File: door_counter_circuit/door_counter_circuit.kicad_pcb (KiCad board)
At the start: 4 copper layers, 99.1 x 99.1 mm, 36 parts, among them J1 Conn_01x20_Male, J2 Conn_01x20_Male, J3 Prototype_Space, Q1 BC807, SW1 SW_Push, SW2 RotaryEncoder_Switch, SW3 SW_Push, U1 Pico, U2 TSDP341xx, U3 TSDP341xx, U4 OLED_display_module, U5 DS1302+, Y1 32.768kHz

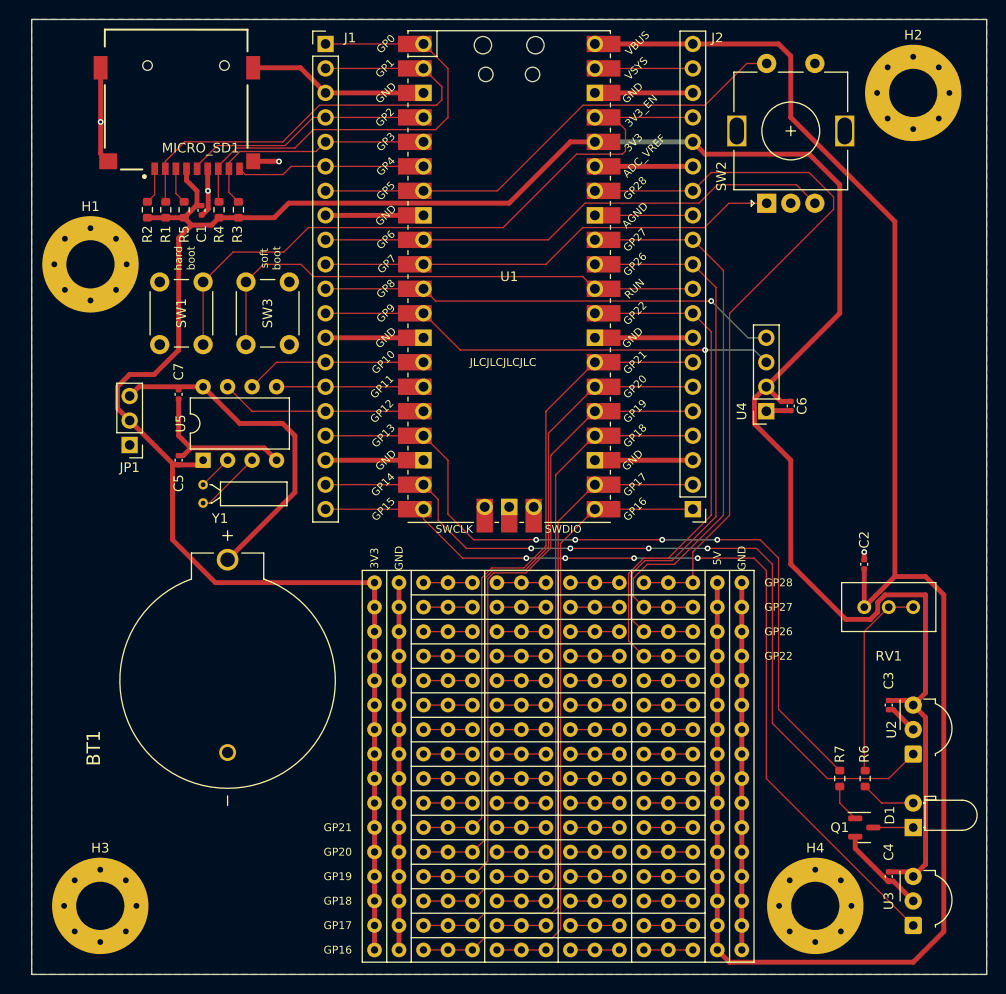
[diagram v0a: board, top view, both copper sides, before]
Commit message: include a configurable transistor footprint
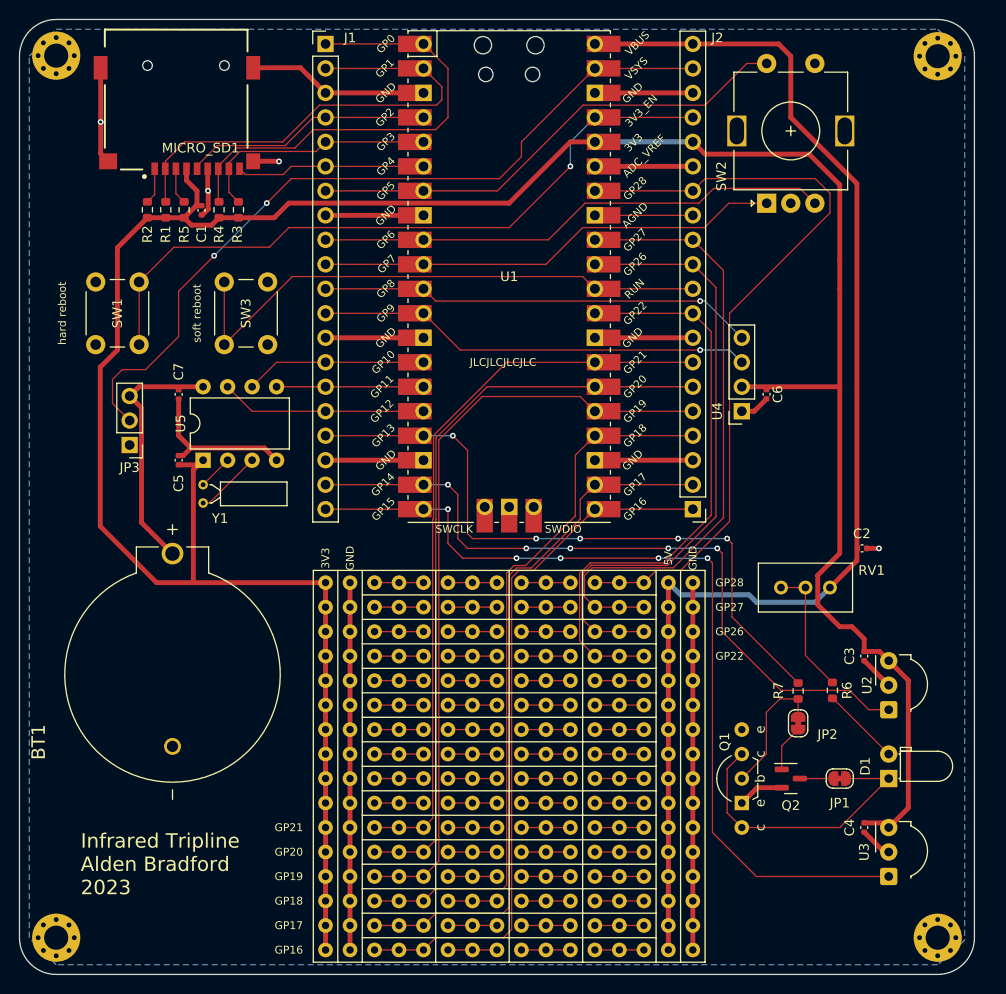
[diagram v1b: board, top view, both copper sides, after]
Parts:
- added JP1: SolderJumper_2_Bridged, Jumper:SolderJumper-2_P1.3mm_Bridged_RoundedPad1.0x1.5mm, F.Cu at (157.5, 129.5)
- added JP2: SolderJumper_2_Bridged, Jumper:SolderJumper-2_P1.3mm_Bridged_RoundedPad1.0x1.5mm, F.Cu at (153.2, 123.8)
- added Q1: ConfigurableNPN, Library:TO-92-configurable, F.Cu at (147.3, 132.1)
- H1, H2, H3, H4: footprint MountingHole:MountingHole_5mm_Pad_Via -> MountingHole:MountingHole_2.5mm_Pad_Via
- moved H1 21.9 mm to (76.2, 54.6)
- moved H4 13.1 mm to (167.6, 146.1)
- moved R7 10.1 mm to (153.2, 120.5)
- moved R6 9.76 mm to (156.7, 120.4)
- moved Q2 9.16 mm to (152.4, 129.5)
- moved SW1 6.64 mm to (84.8, 78.0)
- moved BT1 5.75 mm to (88.3, 116.2)
- moved D1 5.68 mm to (162.6, 129.5)
- moved U3 5.68 mm to (162.6, 139.7)
- moved C3 5.68 mm to (160.0, 116.8)
- moved C4 5.68 mm to (160.0, 134.6)
- moved H3 5.64 mm to (76.2, 146.1)
- moved U2 5.25 mm to (162.6, 122.4)
- moved J3 5.08 mm to (104.1, 147.3)
- moved H2 4.58 mm to (167.6, 54.6)
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- renumbered JP1 to JP3, Q1 to Q2
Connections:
- J2 pad 19: Net-(J2-Pad19) -> VSYS
- JP3 pad 2: +3V3 -> VSYS
- Q2 pad 1: Net-(Q1-Pad1) -> Net-(Q2-Pad1)
- Q2 pad 3: Net-(D1-Pad1) -> Net-(Q2-Pad3)
- R7 pad 2: Net-(Q1-Pad1) -> Net-(R7-Pad2)
- U1 pad 39: Net-(J2-Pad19) -> VSYS
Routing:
- net VSYS: track 0.00 -> 82.2 mm, vias 0 -> 2
- net +5V: track 192.0 -> 136.3 mm
- net Net-(D1-Pad1): track 4.14 -> 30.7 mm
- net Net-(R7-Pad2): track 0.00 -> 13.7 mm
- net IR_CONTROL: track 80.2 -> 69.2 mm, vias 4 -> 5
- net Net-(J2-Pad19): track 10.2 -> 0.00 mm
- net IR_DETECT_1: track 85.6 -> 75.5 mm, vias 4 -> 5
- net Net-(BT1-Pad+): track 35.4 -> 26.2 mm
- net C4: track 70.7 -> 79.9 mm
- net Net-(RV1-Pad2): track 20.6 -> 13.5 mm
- net C5: track 70.7 -> 77.4 mm
- net C6: track 70.7 -> 76.2 mm
- net M15: track 60.6 -> 66.0 mm
- net +3V3: track 290.1 -> 284.9 mm
- net M14: track 60.2 -> 65.3 mm
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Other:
- outline, holes or cut-outs redrawn
- board text added: "Infrared Tripline Alden Bradford 2023"
- board text added: "hard reboot"
- board text added: "soft reboot"
- board text removed: "hard boot"
- board text removed: "soft boot"

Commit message: manufacturing outputs
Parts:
- added FID1: Fiducial, Fiducial:Fiducial_1mm_Mask2mm, F.Cu at (162.6, 54.4)
- added FID2: Fiducial, Fiducial:Fiducial_1mm_Mask2mm, F.Cu at (76.7, 59.4)
- added FID3: Fiducial, Fiducial:Fiducial_1mm_Mask2mm, F.Cu at (76.2, 141.2)
- added FID4: Fiducial, Fiducial:Fiducial_1mm_Mask2mm, F.Cu at (162.6, 145.8)
- added TP1: TestPoint, TestPoint:TestPoint_Pad_4.0x4.0mm, F.Cu at (167.1, 63.5)
- added TP2: TestPoint, TestPoint:TestPoint_Pad_4.0x4.0mm, F.Cu at (89.6, 144.8)
- added TP3: TestPoint, TestPoint:TestPoint_Pad_4.0x4.0mm, F.Cu at (157.2, 145.8)
- Q1: renamed from Q2; value BC807 -> MMS9013-H-TP
- R7: renamed from R6; footprint Resistor_SMD:R_0603_1608Metric -> Resistor_SMD:R_0805_2012Metric
- moved J2 5.08 mm to (137.2, 101.6)
- moved U2 5.08 mm to (142.2, 91.4)
- moved C3 4.85 mm to (145.0, 89.7)
- moved U1 2.54 mm to (120.7, 77.5)
- renumbered C7 to C2, C6 to C3, C5 to C4, C2 to C5, C3 to C6, C4 to C7, JP3 to JP1, JP1 to JP3, Q1 to Q2, R2 to R1, R1 to R2, R5 to R3, R3 to R5, R7 to R6, SW2 to SW1, SW1 to SW2, U4 to U2, U5 to U3, U2 to U4, U3 to U5
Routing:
- net GND: track 206.3 -> 217.6 mm
- net C4: track 79.9 -> 70.1 mm
- net C5: track 77.4 -> 69.4 mm
- net C6: track 76.2 -> 68.6 mm
- net M15: track 66.0 -> 59.0 mm
- net M14: track 65.3 -> 59.0 mm
- net M13: track 62.4 -> 56.4 mm
- net +3V3: track 284.9 -> 290.0 mm
- net Net-(J2-Pad10): track 58.6 -> 53.5 mm
- net OLED_SCL: track 45.3 -> 40.2 mm
- net OLED_SDA: track 45.3 -> 40.2 mm
- net VSYS: track 82.2 -> 77.3 mm
- net IR_CONTROL: track 69.2 -> 64.4 mm, vias 5 -> 1
- net C2: track 73.3 -> 68.8 mm
- net C1: track 73.3 -> 68.8 mm
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
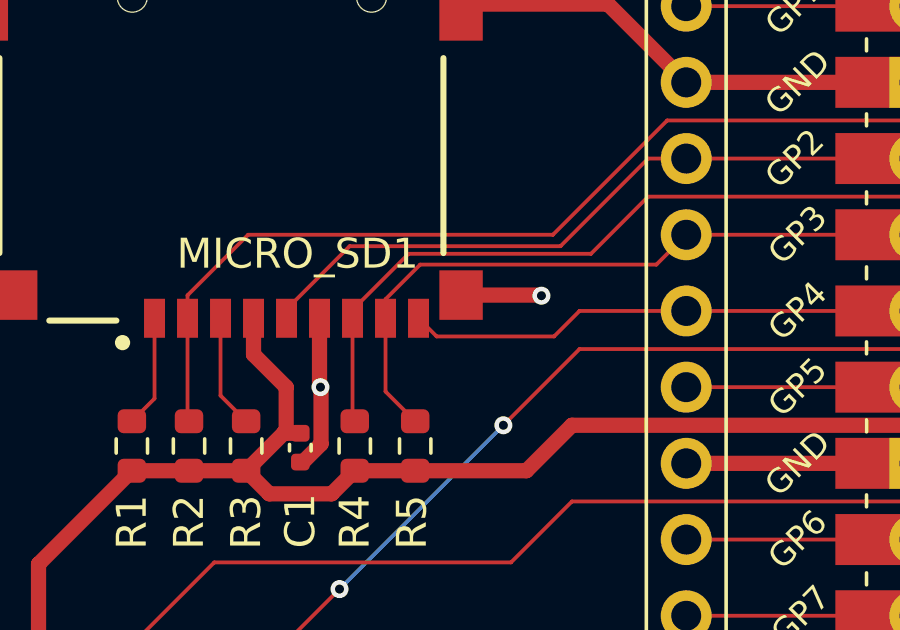
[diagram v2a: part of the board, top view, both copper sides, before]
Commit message: fix to SD circuit
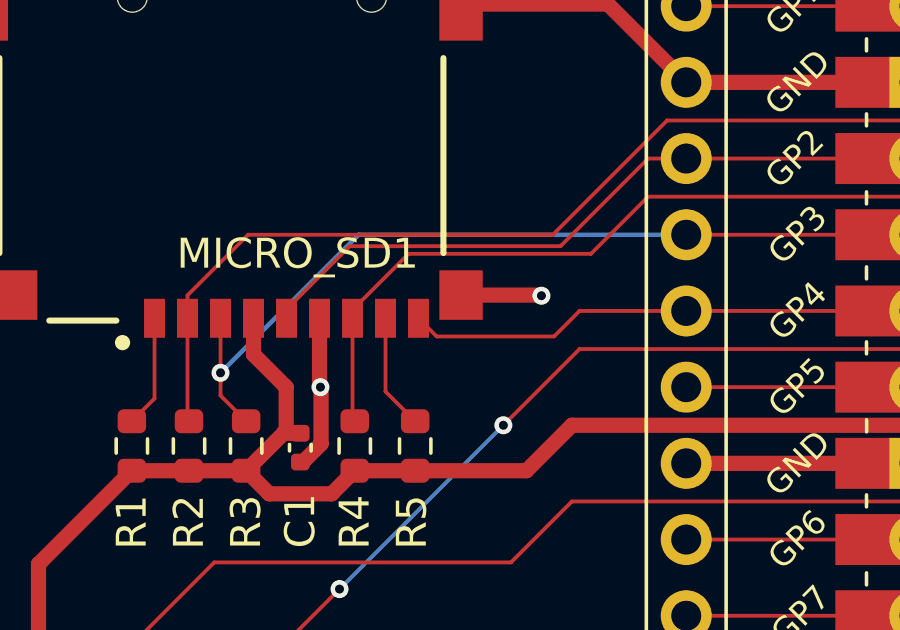
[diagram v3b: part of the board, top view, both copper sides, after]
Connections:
- MICRO_SD1 pad 3: Net-(MICRO_SD1-Pad3) -> SD_MOSI
- MICRO_SD1 pad 8: SD_MOSI -> Net-(MICRO_SD1-Pad8)
- R3 pad 2: Net-(MICRO_SD1-Pad3) -> SD_MOSI
- R5 pad 2: SD_MOSI -> Net-(MICRO_SD1-Pad8)
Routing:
- net SD_MOSI: track 23.0 -> 28.8 mm, vias 0 -> 1
- net Net-(MICRO_SD1-Pad8): track 0.00 -> 3.84 mm
- net Net-(MICRO_SD1-Pad3): track 3.79 -> 0.00 mm
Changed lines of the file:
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@@
   (net 34 "SD_CS")
   (net 35 "Net-(MICRO_SD1-Pad1)")
-  (net 36 "Net-(MICRO_SD1-Pad3)")
+  (net 36 "Net-(MICRO_SD1-Pad8)")
   (net 37 "unconnected-(JP1-Pad1)")
   (net 38 "Net-(JP3-Pad1)")
@@
       (net 34 "SD_CS") (pinfunction "CD/DAT3") (pintype "bidirectional"))
     (pad "3" smd rect locked (at 0.0298 -7.1738 270) (size 1.3 0.7) (layers "F.Cu" "F.Paste" "F.Mask")
-      (net 36 "Net-(MICRO_SD1-Pad3)") (pinfunction "CMD") (pintype "bidirectional"))
+      (net 17 "SD_MOSI") (pinfunction "CMD") (pintype "bidirectional"))
     (pad "4" smd rect locked (at -1.0702 -7.1738 270) (size 1.3 0.7) (layers "F.Cu" "F.Paste" "F.Mask")
       (net 1 "+3V3") (pinfunction "VDD") (pintype "power_in"))
@@
       (net 15 "SD_MISO") (pinfunction "DAT0") (pintype "bidirectional"))
     (pad "8" smd rect locked (at -5.4702 -7.1738 270) (size 1.3 0.7) (layers "F.Cu" "F.Paste" "F.Mask")
-      (net 17 "SD_MOSI") (pinfunction "DAT1") (pintype "bidirectional"))
+      (net 36 "Net-(MICRO_SD1-Pad8)") (pinfunction "DAT1") (pintype "bidirectional"))
     (pad "CD1" smd rect locked (at -6.5702 -7.1738 270) (size 1.3 0.7) (layers "F.Cu" "F.Paste" "F.Mask")
       (net 18 "SD_DET") (pinfunction "CD") (pintype "passive"))
@@
       (net 1 "+3V3") (pintype "passive"))
     (pad "2" smd roundrect (at 0.825 0 90) (size 0.8 0.95) (layers "F.Cu" "F.Paste" "F.Mask") (roundrect_rratio 0.25)
-      (net 36 "Net-(MICRO_SD1-Pad3)") (pintype "passive"))
+      (net 17 "SD_MOSI") (pintype "passive"))
     (model "${KICAD6_3DMODEL_DIR}/Resistor_SMD.3dshapes/R_0603_1608Metric.wrl"
       (offset (xyz 0 0 0))
@@
       (net 1 "+3V3") (pintype "passive"))
     (pad "2" smd roundrect (at 0.825 0 90) (size 0.8 0.95) (layers "F.Cu" "F.Paste" "F.Mask") (roundrect_rratio 0.25)
-      (net 17 "SD_MOSI") (pintype "passive"))
+      (net 36 "Net-(MICRO_SD1-Pad8)") (pintype "passive"))
     (model "${KICAD6_3DMODEL_DIR}/Resistor_SMD.3dshapes/R_0603_1608Metric.wrl"
       (offset (xyz 0 0 0))
@@
   (segment (start 104.14 60.96) (end 111.76 60.96) (width 0.127) (layer "F.Cu") (net 16))
   (segment (start 90.8162 66.2848) (end 90.8162 65.9848) (width 0.127) (layer "F.Cu") (net 16))
-  (segment (start 95.271 64.495) (end 103.145 64.495) (width 0.127) (layer "F.Cu") (net 17))
-  (segment (start 94.1162 68.7262) (end 95.106 69.716) (width 0.127) (layer "F.Cu") (net 17))
-  (segment (start 94.1162 66.2848) (end 94.1162 65.6498) (width 0.127) (layer "F.Cu") (net 17))
-  (segment (start 103.145 64.495) (end 104.14 63.5) (width 0.127) (layer "F.Cu") (net 17))
-  (segment (start 94.1162 65.6498) (end 95.271 64.495) (width 0.127) (layer "F.Cu") (net 17))
-  (segment (start 94.1162 66.2848) (end 94.1162 68.7262) (width 0.127) (layer "F.Cu") (net 17))
+  (segment (start 88.6162 68.1018) (end 88.6162 66.2848) (width 0.127) (layer "F.Cu") (net 17))
+  (segment (start 89.471 69.716) (end 88.6162 68.8612) (width 0.127) (layer "F.Cu") (net 17))
+  (segment (start 88.6162 68.8612) (end 88.6162 68.1018) (width 0.127) (layer "F.Cu") (net 17))
   (segment (start 104.14 63.5) (end 111.76 63.5) (width 0.127) (layer "F.Cu") (net 17))
+  (via (at 88.6162 68.1018) (size 0.6) (drill 0.3) (layers "F.Cu" "B.Cu") (net 17))
+  (segment (start 104.14 63.5) (end 93.218 63.5) (width 0.15) (layer "B.Cu") (net 17))
+  (segment (start 93.218 63.5) (end 88.6162 68.1018) (width 0.15) (layer "B.Cu") (net 17))
   (segment (start 99.734 66.89) (end 100.584 66.04) (width 0.127) (layer "F.Cu") (net 18))
   (segment (start 100.584 66.04) (end 104.14 66.04) (width 0.127) (layer "F.Cu") (net 18))
@@
   (segment (start 86.4162 68.9608) (end 86.4162 66.2848) (width 0.127) (layer "F.Cu") (net 35))
   (segment (start 85.661 69.716) (end 86.4162 68.9608) (width 0.127) (layer "F.Cu") (net 35))
-  (segment (start 89.471 69.716) (end 88.6162 68.8612) (width 0.127) (layer "F.Cu") (net 36))
-  (segment (start 88.6162 68.8612) (end 88.6162 66.2848) (width 0.127) (layer "F.Cu") (net 36))
+  (segment (start 94.1162 68.7262) (end 95.106 69.716) (width 0.127) (layer "F.Cu") (net 36))
+  (segment (start 94.1162 66.2848) (end 94.1162 68.7262) (width 0.127) (layer "F.Cu") (net 36))
   (segment (start 153.3375 129.54) (end 156.83 129.54) (width 0.127) (layer "F.Cu") (net 38))
   (segment (start 129.54 78.74) (end 137.16 78.74) (width 0.127) (layer "F.Cu") (net 39))
